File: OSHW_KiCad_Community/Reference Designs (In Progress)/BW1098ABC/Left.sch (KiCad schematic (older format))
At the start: 15 parts, among them J7 BBR43-24KB533 for camera modu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

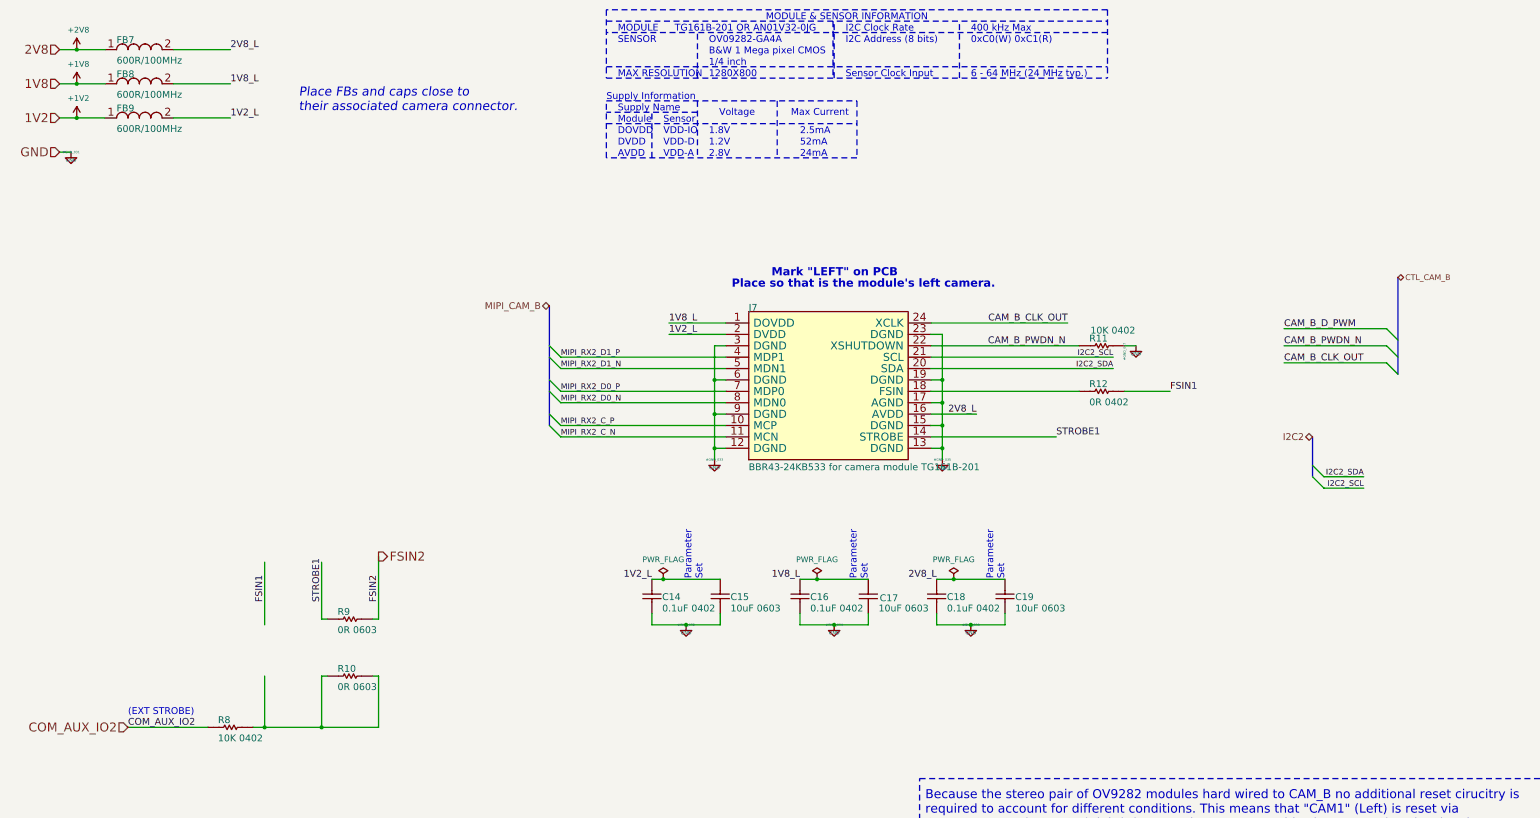
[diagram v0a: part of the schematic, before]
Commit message: BW1098ABC - added back in usbc, got rid of hierarchical labeling in favor of globals. Passes ERC
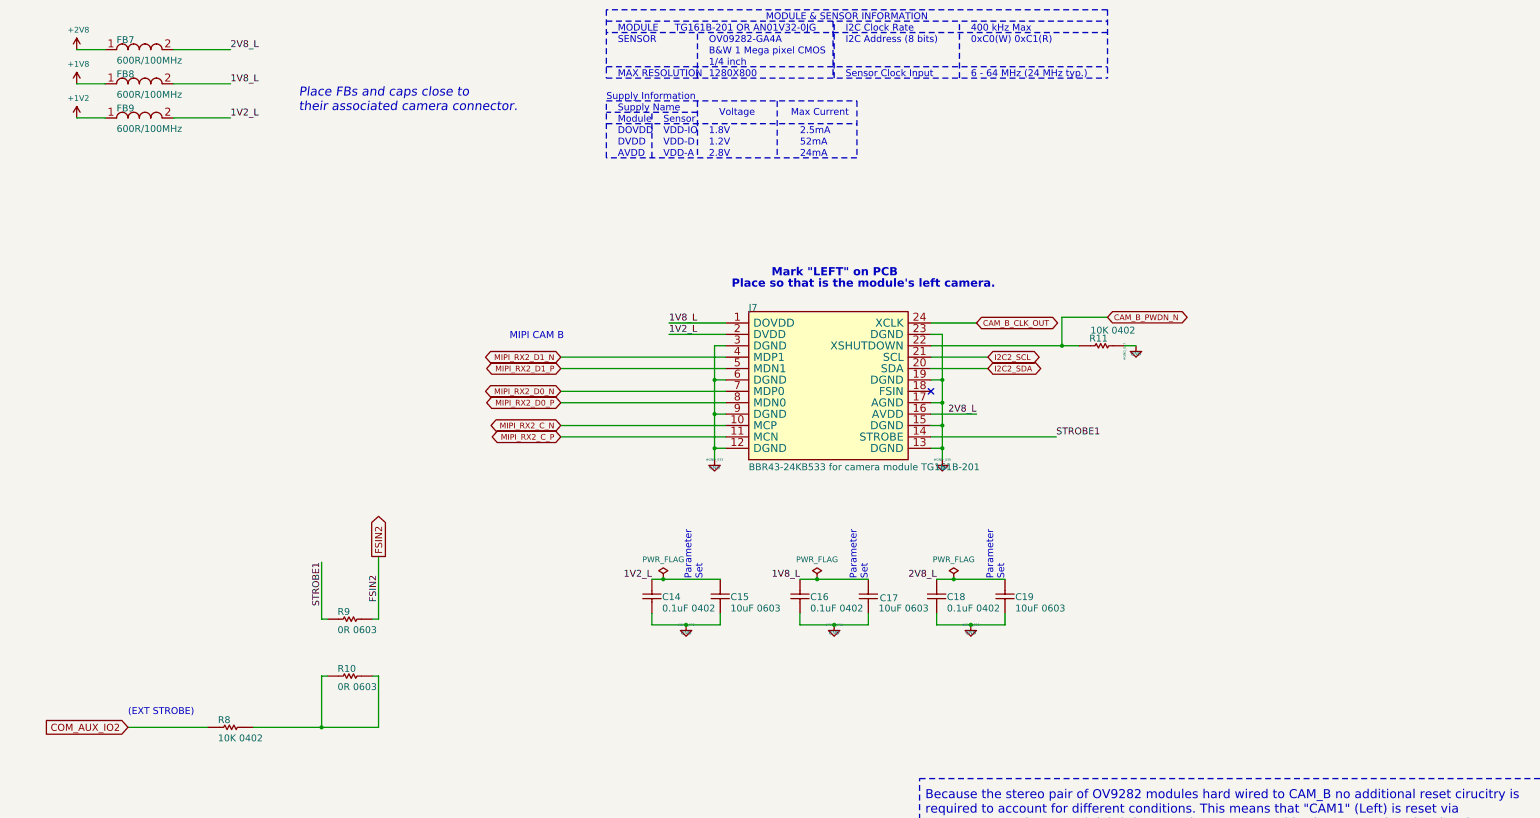
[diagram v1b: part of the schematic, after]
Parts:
- removed R12: 0R 0402, Resistor_SMD:R_0402_1005Metric, symbol BW1098ABC-rescue:CRCW04020000Z0ED-depthAI_sch
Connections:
- net labels removed: 1V2, 1V8, 2V8, CAM_B_D_PWM, CTL_CAM_B, FSIN1, I2C2, MIPI_CAM_B
- wire segments 82 -> 71
- no-connect marks 0 -> 1
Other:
- note added: "MIPI CAM B"
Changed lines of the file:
@@
 $Descr A3 16535 11693
 encoding utf-8
-Sheet 6 6
+Sheet 6 7
 Title ""
 Date ""
@@
 	1    0    0    -1
 $EndComp
-Text Label 1500 6850 0    60   ~ 0
-COM_AUX_IO2
-Text Label 2700 5750 1    60   ~ 0
-FSIN1
-Text Label 3200 5750 1    60   ~ 0
+Text Label 3200 5400 3    60   ~ 0
 STROBE1
 Text Label 3700 5750 1    60   ~ 0
@@
 Text Notes 1500 6750 0    60   ~ 0
 (EXT STROBE)
-Text Label 9750 3300 2    60   ~ 0
-CAM_B_CLK_OUT
-Text Label 9050 3500 0    60   ~ 0
-CAM_B_PWDN_N
 $Comp
 L power:GND #GND_?
@@
 F 3 "" H 6650 4500 70  0000 C CNN
 	1    6650 4500
-	1    0    0    -1
-$EndComp
-$Comp
-L power:GND #GND_?
-U 1 1 603D7ABB
-P 1000 1800
-AR Path="/5FD7EFD3/603D7ABB" Ref="#GND_?"  Part="1"
-AR Path="/5FF8D2B3/603D7ABB" Ref="#GND_031"  Part="1"
-F 0 "#GND_031" H 1000 1800 20  0000 C CNN
-F 1 "GND" H 1000 1730 30  0000 C CNN
-F 2 "" H 1000 1800 70  0000 C CNN
-F 3 "" H 1000 1800 70  0000 C CNN
-	1    1000 1800
 	1    0    0    -1
 $EndComp
@@
 	6700 5850 6700 5950
 Wire Wire Line
-	9850 3500 8550 3500
+	9850 3500 9700 3500
 Wire Wire Line
 	9650 4300 8550 4300
@@
 	8650 3800 8550 3800
 Wire Wire Line
-	1000 1800 900  1800
-Wire Wire Line
 	6750 3300 6250 3300
 Wire Wire Line
@@
 	3200 6850 3700 6850
 Wire Wire Line
-	2700 6850 3200 6850
-Wire Wire Line
-	2600 6850 2700 6850
-Wire Wire Line
-	8550 3900 9850 3900
-Wire Wire Line
 	9200 5950 8900 5950
 Wire Wire Line
@@
 	3250 6400 3200 6400
 Wire Wire Line
-	2700 6850 2700 6400
-Wire Wire Line
 	3700 5900 3650 5900
-Connection ~ 2700 6850
 Connection ~ 3200 6850
 Connection ~ 6400 5950
@@
 F 3 "" H 9940 3370 60  0000 C CNN
 	1    9850 3500
-	1    0    0    -1
-$EndComp
-$Comp
-L BW1098ABC-rescue:CRCW04020000Z0ED-depthAI_sch R?
-U 1 1 603D7BA2
-P 9850 3900
-AR Path="/5FD7EFD3/603D7BA2" Ref="R?"  Part="1"
-AR Path="/5FF8D2B3/603D7BA2" Ref="R12"  Part="1"
-F 0 "R12" H 9940 3930 60  0000 L BNN
-F 1 "0R 0402" H 9940 3770 60  0000 L BNN
-F 2 "Resistor_SMD:R_0402_1005Metric" H 9940 3770 60  0001 C CNN
-F 3 "" H 9940 3770 60  0000 C CNN
-	1    9850 3900
 	1    0    0    -1
 $EndComp
@@
 EndData
 $EndBitmap
-Wire Wire Line
-	900  900  1050 900
-Wire Wire Line
-	900  1500 1050 1500
 Text Notes 3000 1450 0    79   Italic 0
 Place FBs and caps close to \ntheir associated camera connector.
-Wire Wire Line
-	10650 3900 10250 3900
-Text Label 10650 3900 0    60   ~ 0
-FSIN1
 Text Notes 6550 5550 1    60   ~ 0
 Parameter \nSet\n
-Wire Wire Line
-	8550 3700 10150 3700
 $Comp
 L power:+1V2 #PWR?
@@
 	1    0    0    -1
 $EndComp
-Connection ~ 1050 900
 Wire Wire Line
 	1050 900  1300 900
-Connection ~ 1050 1200
 Wire Wire Line
 	1050 1200 1300 1200
 Wire Wire Line
-	900  1200 1050 1200
-Connection ~ 1050 1500
-Wire Wire Line
 	1050 1500 1300 1500
-Wire Wire Line
-	8550 3600 10150 3600
-Text Label 10150 3600 2    49   ~ 0
-I2C2_SCL
-Text Label 10150 3700 2    49   ~ 0
-I2C2_SDA
 Text Notes 8000 5550 1    60   ~ 0
 Parameter \nSet\n
@@
 	8750 5550 8600 5550
 Wire Wire Line
-	2700 5400 2700 5950
-Text HLabel 3700 5350 2    79   Output ~ 0
-FSIN2
-Text HLabel 900  900  0    79   Input ~ 0
-2V8
-Text HLabel 900  1200 0    79   Input ~ 0
-1V8
-Text HLabel 900  1500 0    79   Input ~ 0
-1V2
-Text HLabel 900  1800 0    79   Input ~ 0
-GND
-Text HLabel 1500 6850 0    79   Input ~ 0
-COM_AUX_IO2
-Text HLabel 5200 3150 0    60   BiDi ~ 0
-MIPI_CAM_B
-Entry Wire Line
-	5200 4200 5300 4300
-Entry Wire Line
-	5200 4100 5300 4200
-Entry Wire Line
-	5200 3900 5300 4000
-Entry Wire Line
-	5200 3800 5300 3900
-Entry Wire Line
-	5200 3600 5300 3700
-Entry Wire Line
-	5200 3500 5300 3600
-Text Label 5300 3700 0    50   ~ 0
-MIPI_RX2_D1_N
-Text Label 5300 3600 0    50   ~ 0
-MIPI_RX2_D1_P
-Text Label 5300 4000 0    50   ~ 0
-MIPI_RX2_D0_N
-Text Label 5300 3900 0    50   ~ 0
-MIPI_RX2_D0_P
-Text Label 5300 4300 0    50   ~ 0
-MIPI_RX2_C_N
-Text Label 5300 4200 0    50   ~ 0
-MIPI_RX2_C_P
-Wire Wire Line
 	5300 4300 6750 4300
 Wire Wire Line
@@
 Wire Wire Line
 	5300 3600 6750 3600
-Text Label 12350 4650 2    50   ~ 0
-I2C2_SDA
-Text Label 12350 4750 2    50   ~ 0
-I2C2_SCL
-Entry Wire Line
-	11900 4650 12000 4750
-Entry Wire Line
-	11900 4550 12000 4650
-Wire Wire Line
-	12000 4650 12350 4650
-Wire Wire Line
-	12350 4750 12000 4750
 Text Label 2400 900  0    60   ~ 0
 2V8_L
@@
 2V8_L
 Wire Wire Line
-	8550 3300 9750 3300
-Text Label 11650 3350 0    60   ~ 0
-CAM_B_D_PWM
-Entry Wire Line
-	12550 3350 12650 3450
-Wire Wire Line
-	11650 3350 12550 3350
-Text Label 11650 3650 0    60   ~ 0
-CAM_B_CLK_OUT
-Text HLabel 12650 2900 2    50   BiDi ~ 0
-CTL_CAM_B
-Entry Wire Line
-	12550 3650 12650 3750
-Entry Wire Line
-	12550 3500 12650 3600
-Wire Wire Line
-	12550 3650 11650 3650
-Wire Wire Line
-	12550 3500 11650 3500
-Text Label 11650 3500 0    60   ~ 0
-CAM_B_PWDN_N
-Text HLabel 11900 4300 0    60   BiDi ~ 0
-I2C2
-Wire Wire Line
 	1900 900  2400 900
 Wire Wire Line
@@
 Text Label 8600 5550 2    60   ~ 0
 2V8_L
-Wire Bus Line
-	11900 4300 11900 4650
-Wire Bus Line
-	12650 2900 12650 3750
-Wire Bus Line
-	5200 3150 5200 4200
+Text GLabel 5300 3600 0    50   BiDi ~ 0
+MIPI_RX2_D1_N
+Text GLabel 5300 3700 0    50   BiDi ~ 0
+MIPI_RX2_D1_P
+Text GLabel 5300 3900 0    50   BiDi ~ 0
+MIPI_RX2_D0_N
+Text GLabel 5300 4000 0    50   BiDi ~ 0
+MIPI_RX2_D0_P
+Text GLabel 5300 4200 0    50   BiDi ~ 0
+MIPI_RX2_C_N
+Text GLabel 5300 4300 0    50   BiDi ~ 0
+MIPI_RX2_C_P
+Text GLabel 9050 3700 2    50   BiDi ~ 0
+I2C2_SDA
+Text GLabel 9050 3600 2    50   BiDi ~ 0
+I2C2_SCL
+Text GLabel 10100 3250 2    50   BiDi ~ 0
+CAM_B_PWDN_N
+Text GLabel 8950 3300 2    50   BiDi ~ 0
+CAM_B_CLK_OUT
+Text Notes 4850 3450 0    62   ~ 0
+MIPI CAM B
+Wire Wire Line
+	8950 3300 8550 3300
+Wire Wire Line
+	9700 3500 9700 3250
+Wire Wire Line
+	9700 3250 10100 3250
+Connection ~ 9700 3500
+Wire Wire Line
+	9700 3500 8550 3500
+Wire Wire Line
+	9050 3600 8550 3600
+Wire Wire Line
+	9050 3700 8550 3700
+Text GLabel 3700 5350 1    62   Output ~ 0
+FSIN2
+Wire Wire Line
+	2600 6850 3200 6850
+Text GLabel 1500 6850 0    62   Input ~ 0
+COM_AUX_IO2
+NoConn ~ 8550 3900
 $EndSCHEMATC

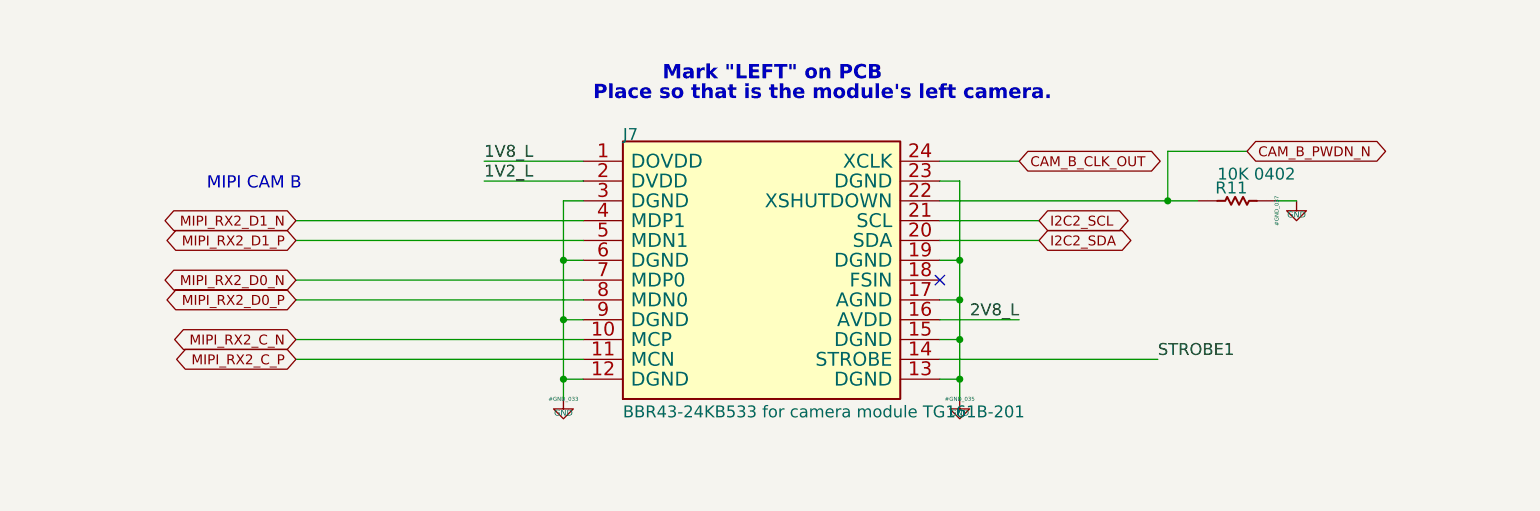
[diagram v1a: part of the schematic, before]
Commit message: going through footprints and datasheet stuff
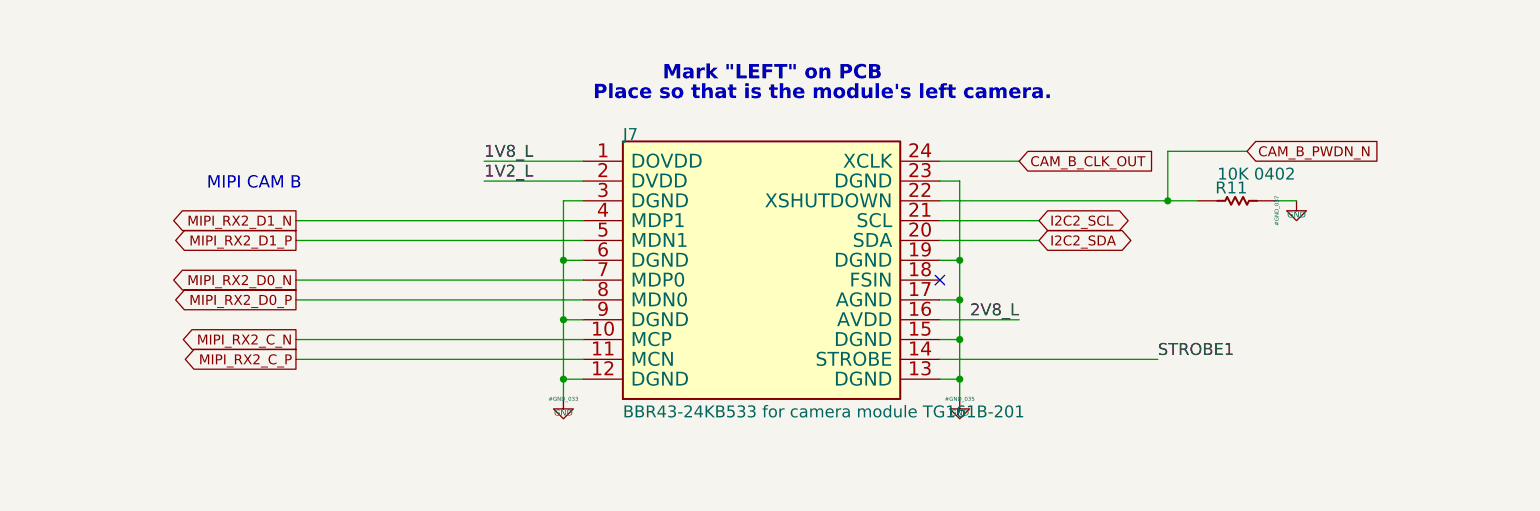
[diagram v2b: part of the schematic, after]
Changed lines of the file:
@@
 Text Label 8600 5550 2    60   ~ 0
 2V8_L
-Text GLabel 5300 3600 0    50   BiDi ~ 0
+Text GLabel 5300 3600 0    50   Output ~ 0
 MIPI_RX2_D1_N
-Text GLabel 5300 3700 0    50   BiDi ~ 0
+Text GLabel 5300 3700 0    50   Output ~ 0
 MIPI_RX2_D1_P
-Text GLabel 5300 3900 0    50   BiDi ~ 0
+Text GLabel 5300 3900 0    50   Output ~ 0
 MIPI_RX2_D0_N
-Text GLabel 5300 4000 0    50   BiDi ~ 0
+Text GLabel 5300 4000 0    50   Output ~ 0
 MIPI_RX2_D0_P
-Text GLabel 5300 4200 0    50   BiDi ~ 0
+Text GLabel 5300 4200 0    50   Output ~ 0
 MIPI_RX2_C_N
-Text GLabel 5300 4300 0    50   BiDi ~ 0
+Text GLabel 5300 4300 0    50   Output ~ 0
 MIPI_RX2_C_P
 Text GLabel 9050 3700 2    50   BiDi ~ 0
@@
 Text GLabel 9050 3600 2    50   BiDi ~ 0
 I2C2_SCL
-Text GLabel 10100 3250 2    50   BiDi ~ 0
+Text GLabel 10100 3250 2    50   Input ~ 0
 CAM_B_PWDN_N
-Text GLabel 8950 3300 2    50   BiDi ~ 0
+Text GLabel 8950 3300 2    50   Input ~ 0
 CAM_B_CLK_OUT
 Text Notes 4850 3450 0    62   ~ 0

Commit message: both camera connector footprints completed
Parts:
- FB7, FB8, FB9: footprint OSHW_LuxonisMaster_20201223:2508056017Y2 -> Luxonis_Kicad_Master:2508056017Y2
- J7: footprint (none) -> Luxonis_Kicad_Master:ACON_BBR43-24KB533
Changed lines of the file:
@@
 F 0 "FB7" H 1400 950 60  0000 L BNN
 F 1 "600R/100MHz" H 1400 770 60  0000 L BNN
-F 2 "OSHW_LuxonisMaster_20201223:2508056017Y2" H 1400 770 60  0001 C CNN
+F 2 "Luxonis_Kicad_Master:2508056017Y2" H 1400 770 60  0001 C CNN
 F 3 "" H 1400 770 60  0000 C CNN
 	1    1300 900
@@
 F 0 "J7" H 6950 3400 60  0000 L BNN
 F 1 "BBR43-24KB533 for camera module TG161B-201" H 6950 2000 60  0000 L BNN
-F 2 "" H 6950 2000 60  0001 C CNN
+F 2 "Luxonis_Kicad_Master:ACON_BBR43-24KB533" H 6950 2000 60  0001 C CNN
 F 3 "" H 6950 2000 60  0000 C CNN
 	1    6750 3300
@@
 F 0 "FB8" H 1400 1250 60  0000 L BNN
 F 1 "600R/100MHz" H 1400 1070 60  0000 L BNN
-F 2 "OSHW_LuxonisMaster_20201223:2508056017Y2" H 1400 1070 60  0001 C CNN
+F 2 "Luxonis_Kicad_Master:2508056017Y2" H 1400 1070 60  0001 C CNN
 F 3 "" H 1400 1070 60  0000 C CNN
 	1    1300 1200
@@
 F 0 "FB9" H 1400 1550 60  0000 L BNN
 F 1 "600R/100MHz" H 1400 1370 60  0000 L BNN
-F 2 "OSHW_LuxonisMaster_20201223:2508056017Y2" H 1400 1370 60  0001 C CNN
+F 2 "Luxonis_Kicad_Master:2508056017Y2" H 1400 1370 60  0001 C CNN
 F 3 "" H 1400 1370 60  0000 C CNN
 	1    1300 1500
